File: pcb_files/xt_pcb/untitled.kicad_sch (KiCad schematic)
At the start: 181 parts, among them SW1 SW_Push, SW10 SW_Push, SW11 SW_Push, SW12 SW_Push, SW13 SW_Push, SW14 SW_Push, SW15 SW_Push, SW16 SW_Push, SW17 SW_Push, SW18 SW_Push, SW19 SW_Push, SW2 SW_Push, SW20 SW_Push, SW21 SW_Push, SW22 SW_Push, SW23 SW_Push, SW24 SW_Push, SW25 SW_Push, SW26 SW_Push, SW27 SW_Push, SW28 SW_Push, SW29 SW_Push, SW3 SW_Push, SW30 SW_Push, SW31 SW_Push, SW32 SW_Push, SW33 SW_Push, SW34 SW_Push, SW35 SW_Push, SW36 SW_Push, SW37 SW_Push, SW38 SW_Push, SW39 SW_Push, SW4 SW_Push, SW40 SW_Push, SW41 SW_Push, SW42 SW_Push, SW43 SW_Push, SW44 SW_Push, SW45 SW_Push, SW46 SW_Push, SW47 SW_Push, SW48 SW_Push, SW49 SW_Push, SW5 SW_Push, SW50 SW_Push, SW51 SW_Push, SW52 SW_Push, SW53 SW_Push, SW54 SW_Push, SW55 SW_Push, SW56 SW_Push, SW57 SW_Push, SW58 SW_Push, SW59 SW_Push, SW6 SW_Push, SW60 SW_Push, SW61 SW_Push, SW62 SW_Push, SW63 SW_Push, SW64 SW_Push, SW66 SW_Push, SW67 SW_Push, SW68 SW_Push, SW69 SW_Push, SW7 SW_Push, SW70 SW_Push, SW71 SW_Push, SW72 SW_Push, SW73 SW_Push, SW74 SW_Push, SW75 SW_Push, SW76 SW_Push, SW77 SW_Push, SW78 SW_Push, SW79 SW_Push, SW8 SW_Push, SW80 SW_Push, SW81 SW_Push, SW82 SW_Push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

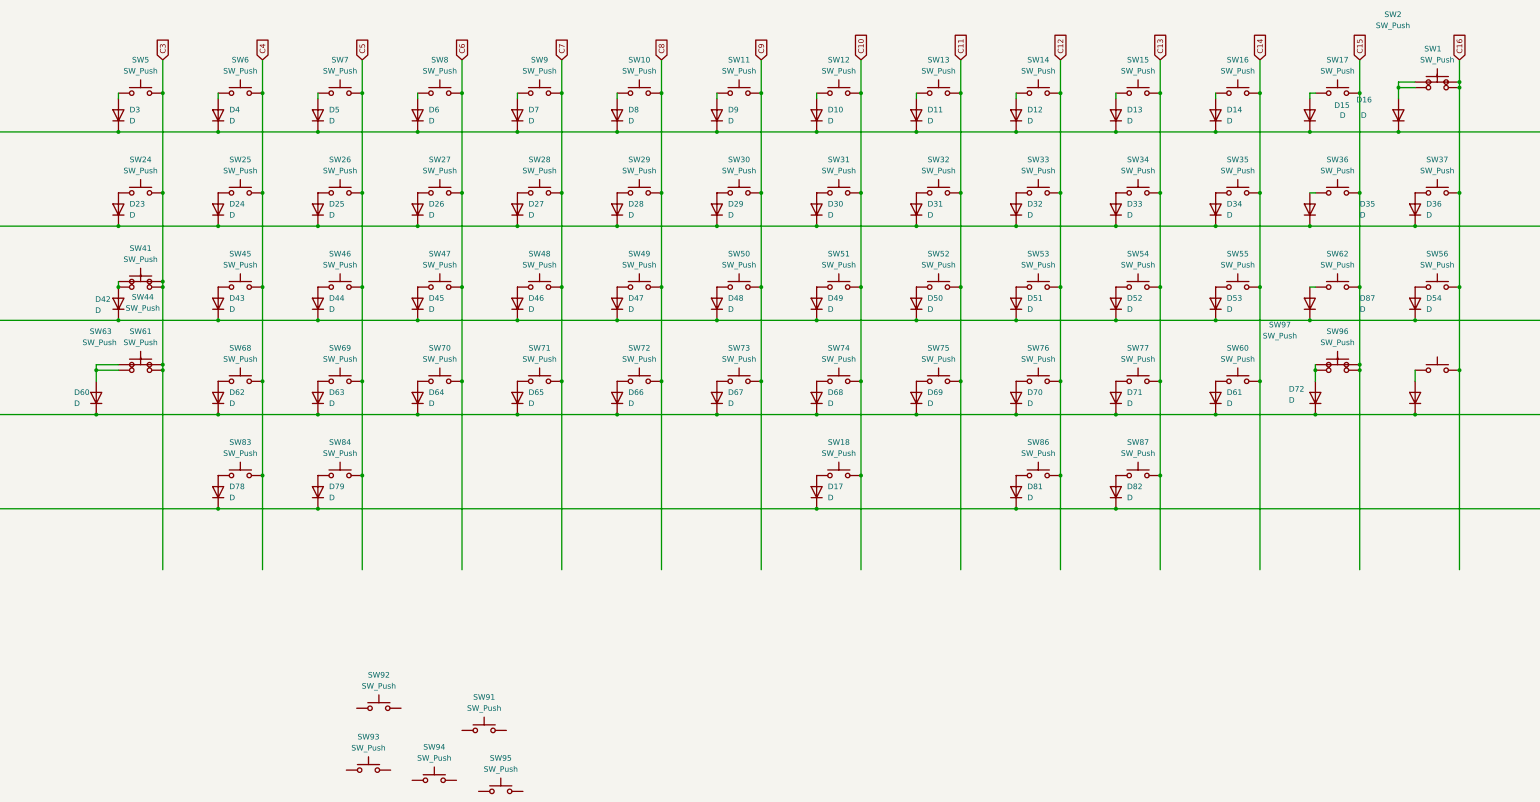
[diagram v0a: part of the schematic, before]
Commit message: connected connected the switch matrix to gpio
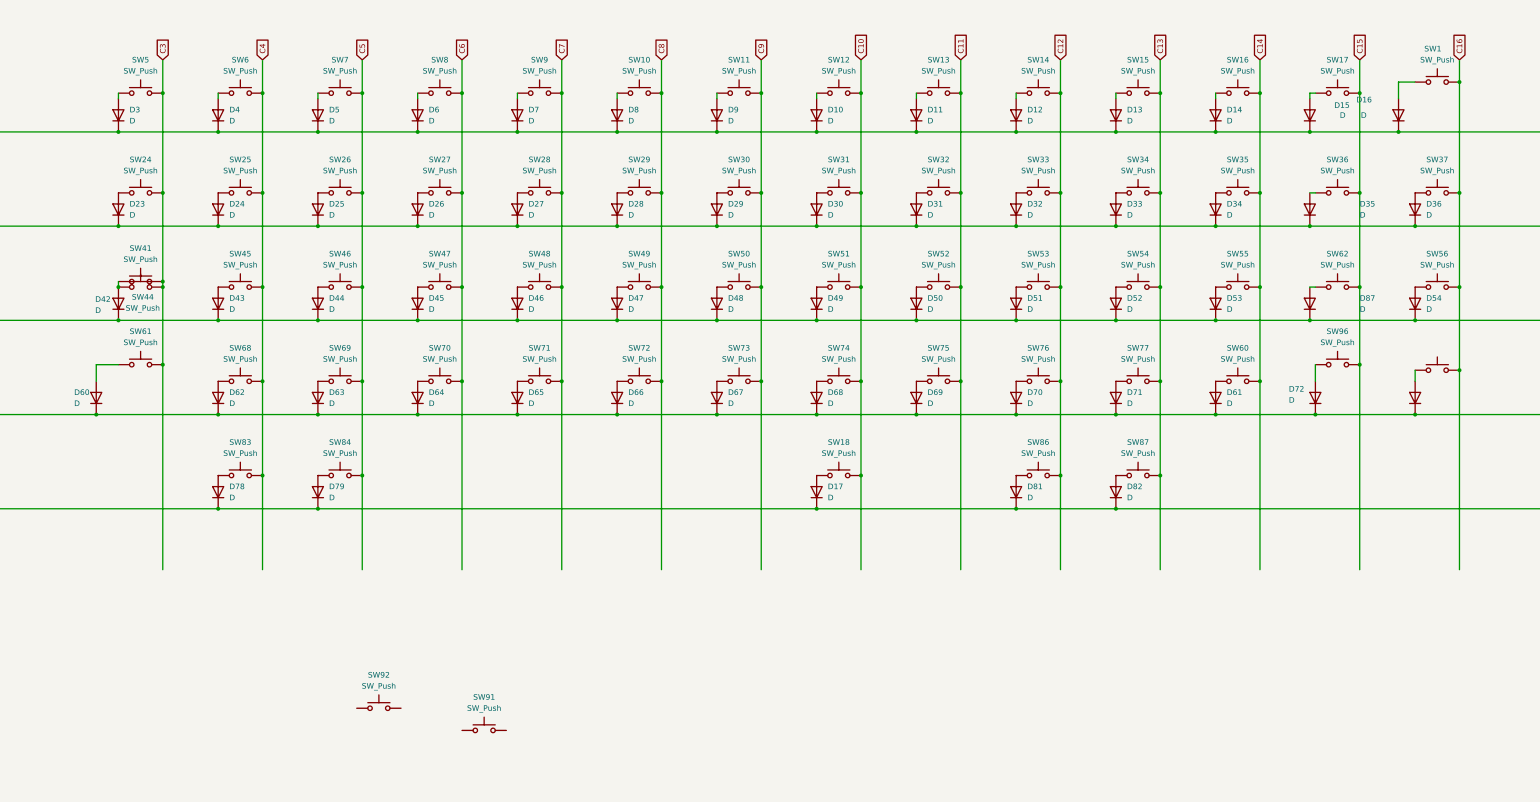
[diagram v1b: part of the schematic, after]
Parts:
- removed SW2: SW_Push, PCM_Switch_Keyboard_Hotswap_Kailh:SW_Hotswap_Kailh_MX_Plated_1.00u, symbol Switch:SW_Push
- removed SW63: SW_Push, PCM_Switch_Keyboard_Hotswap_Kailh:SW_Hotswap_Kailh_MX_Plated_1.25u, symbol Switch:SW_Push
- removed SW93, SW94, SW95: SW_Push, PCM_Mounting_Keyboard_Stabilizer:Stabilizer_Cherry_MX_2.00u, symbol Switch:SW_Push
- removed SW97: SW_Push, PCM_Switch_Keyboard_Hotswap_Kailh:SW_Hotswap_Kailh_MX_Plated_1.75u, symbol Switch:SW_Push
